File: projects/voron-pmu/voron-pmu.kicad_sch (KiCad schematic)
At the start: 11 parts, among them J1 Critical loads, J2 Non-critical loads, J3 Critical supply, J4 Non-critical supply, K1 FINDER-40.52, K2 FINDER-40.52, K3 FINDER-40.52, K4 FINDER-40.52, SW1 SW_Push, SW2 SW_Push_Open

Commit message: Playing around.
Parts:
- added J5: Pwr-loss-1, Connector_JST:JST_XH_B3B-XH-A_1x03_P2.50mm_Vertical, symbol Connector:Conn_01x03_Pin
- added J6: Pwr-loss-2, Connector_Phoenix_MC:PhoenixContact_MCV_1,5_3-G-3.5_1x03_P3.50mm_Vertical, symbol Connector:Conn_01x03_Pin
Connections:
- net at K4.11: now also J5.2 (Pin_2)
- net at K4.12: now also J5.3 (Pin_3)
- net at K4.14: now also J5.1 (Pin_1)
- net at K4.21: now also J6.2 (Pin_2)
- net at K4.22: now also J6.3 (Pin_3)
- net at K4.24: now also J6.1 (Pin_1)
- net at PS2.5 (AC(L)): now also J3.1 (Pin_1), K1.11
- net at PS2.6 (AC(N)): now also J3.2 (Pin_2), K1.21

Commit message: Prettyfing schematics.
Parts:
- added H1, H2, H3, H4: MountingHole, MountingHole:MountingHole_3.2mm_M3, symbol Mechanical:MountingHole
- J6: footprint Connector_Phoenix_MC:PhoenixContact_MCV_1,5_3-G-3.5_1x03_P3.50mm_Vertical -> Connector_JST:JST_XH_B3B-XH-A_1x03_P2.50mm_Vertical
- SW1: value SW_Push -> sw-on; footprint Connector_Phoenix_MC:PhoenixContact_MCV_1,5_2-G-3.5_1x02_P3.50mm_Vertical -> Connector_JST:JST_XH_B2B-XH-A_1x02_P2.50mm_Vertical
- SW2: value SW_Push_Open -> sw-off; footprint Connector_Phoenix_MC:PhoenixContact_MCV_1,5_2-G-3.5_1x02_P3.50mm_Vertical -> Connector_JST:JST_XH_B2B-XH-A_1x02_P2.50mm_Vertical
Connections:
- net at J3.1 (Pin_1), K1.11: now also PS2.6 (AC(N)); no longer PS2.5 (AC(L))
- net at J3.2 (Pin_2), K1.21: now also PS2.5 (AC(L)); no longer PS2.6 (AC(N))
- net power-good renamed +24V-sw
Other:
- note added: "Critical loads"
- note added: "Low-voltage supply"
- note added: "Main power on/off switching"
- note added: "Non-critical loads and detection"
- moved on the sheet: J1, J2, J3, J4, J5, J6, K1, K2, K3, K4, PS2, SW1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

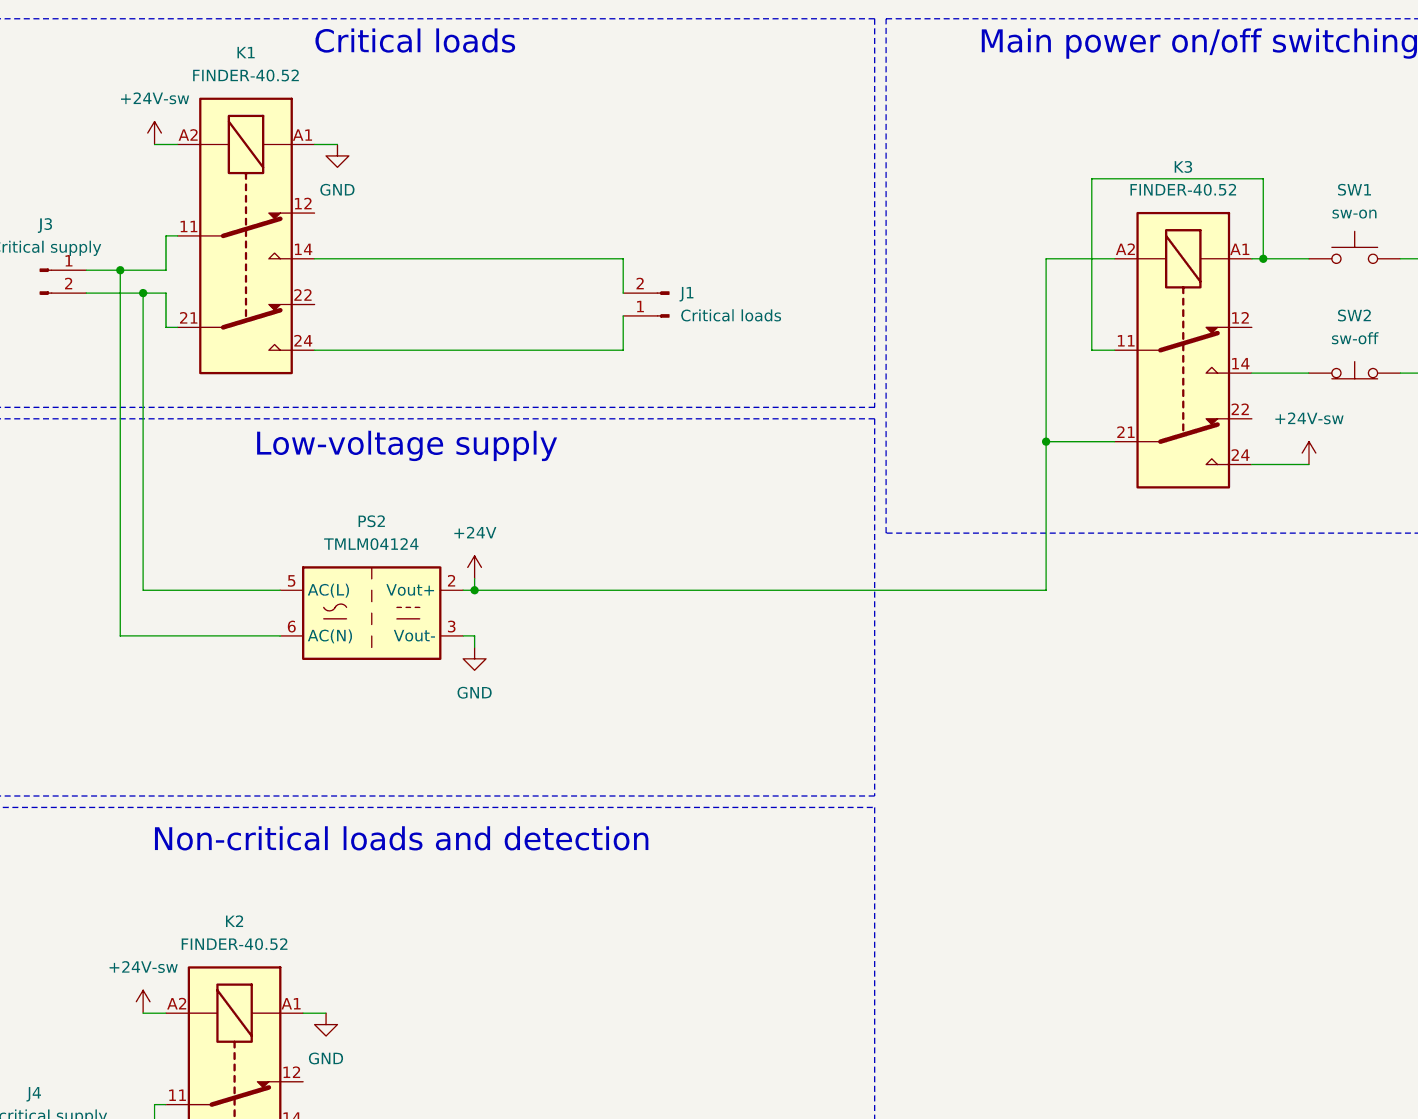
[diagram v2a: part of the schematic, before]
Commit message: Replacing relays with Omron. Will route now.
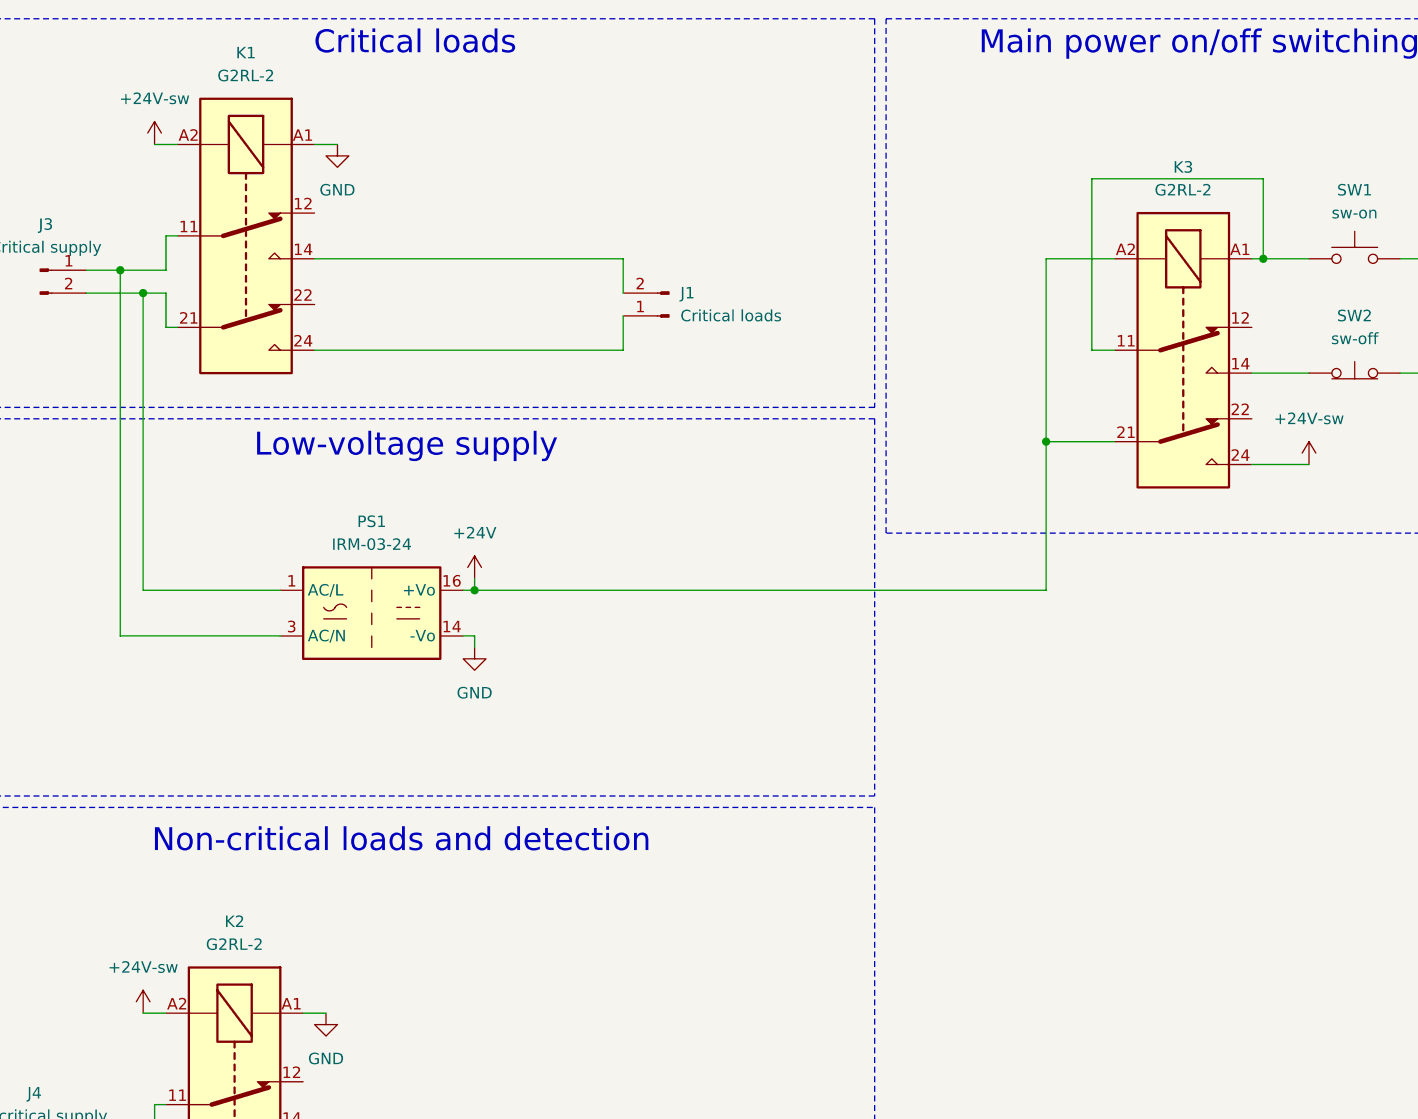
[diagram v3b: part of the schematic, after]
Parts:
- K1, K2, K3: value FINDER-40.52 -> G2RL-2; footprint Relay_THT:Relay_DPDT_Finder_40.52 -> Relay_THT:Relay_DPDT_Omron_G2RL-2; symbol Relay:FINDER-40.52 -> Relay:G2RL-2
- PS1: renamed from PS2; value TMLM04124 -> IRM-03-24; footprint Converter_ACDC:Converter_ACDC_TRACO_TMLM-04_THT -> Converter_ACDC:Converter_ACDC_MeanWell_IRM-03-xx_THT; symbol Converter_ACDC:TMLM04124 -> Converter_ACDC:IRM-03-24
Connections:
- net +24V: now also PS1.16 (+Vo); no longer PS1.2 (Vout+)
- net GND: now also PS1.14 (-Vo); no longer PS1.3 (Vout-)
- net at J3.2 (Pin_2), K1.21: now also PS1.1 (AC/L); no longer PS1.5 (AC(L))
- net at J3.1 (Pin_1), K1.11: now also PS1.3 (AC/N); no longer PS1.6 (AC(N))
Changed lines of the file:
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@@
 	)
 	(symbol
-		(lib_id "Converter_ACDC:TMLM04124")
+		(lib_id "Converter_ACDC:IRM-03-24")
 		(at 63.5 82.55 0)
 		(unit 1)
@@
 		(dnp no)
 		(fields_autoplaced yes)
-		(property "Reference" "PS2"
+		(property "Reference" "PS1"
 			(at 63.5 72.39 0)
 			(effects
@@
 			)
 		)
-		(property "Value" "TMLM04124"
+		(property "Value" "IRM-03-24"
 			(at 63.5 74.93 0)
 			(effects
@@
 			)
 		)
-		(property "Footprint" "Converter_ACDC:Converter_ACDC_TRACO_TMLM-04_THT"
+		(property "Footprint" "Converter_ACDC:Converter_ACDC_MeanWell_IRM-03-xx_THT"
 			(at 63.5 91.44 0)
 			(effects
@@
 			)
 		)
-		(property "Datasheet" "https://www.tracopower.com/products/tmlm.pdf"
+		(property "Datasheet" "https://www.meanwell.com/Upload/PDF/IRM-03/IRM-03-SPEC.PDF"
+			(at 63.5 92.71 0)
+			(effects
+				(font
+					(size 1.27 1.27)
+				)
+				(hide yes)
+			)
+		)
+		(property "Description" "24V, 125mA, 3W, Isolated, AC-DC, IRM03"
 			(at 63.5 82.55 0)
 			(effects
@@
 			)
 		)
-		(property "Description" "24V 167mA AC/DC low noise power module"
-			(at 63.5 82.55 0)
-			(effects
-				(font
-					(size 1.27 1.27)
-				)
-				(hide yes)
-			)
-		)
 		(pin "3"
 		)
-		(pin "2"
-		)
-		(pin "6"
+		(pin "1"
+		)
+		(pin "16"
 		)
 		(pin "5"
 		)
-		(instances
-			(project "voron-pmu"
-				(path "/2cf7b3ca-ad8f-4a14-9215-f0584bf5d4a1"
-					(reference "PS2")
+		(pin "14"
+		)
+		(instances
+			(project "voron-pmu"
+				(path "/2cf7b3ca-ad8f-4a14-9215-f0584bf5d4a1"
+					(reference "PS1")
 					(unit 1)
 				)
@@
 	)
 	(symbol
-		(lib_id "Relay:FINDER-40.52")
+		(lib_id "Relay:G2RL-2")
 		(at 48.26 137.16 270)
 		(unit 1)
@@
 			)
 		)
-		(property "Value" "FINDER-40.52"
+		(property "Value" "G2RL-2"
 			(at 48.26 119.38 90)
 			(effects
@@
 			)
 		)
-		(property "Footprint" "Relay_THT:Relay_DPDT_Finder_40.52"
-			(at 47.498 171.45 0)
-			(effects
-				(font
-					(size 1.27 1.27)
-				)
-				(hide yes)
-			)
-		)
-		(property "Datasheet" "http://gfinder.findernet.com/assets/Series/353/S40EN.pdf"
+		(property "Footprint" "Relay_THT:Relay_DPDT_Omron_G2RL-2"
+			(at 46.99 153.67 0)
+			(effects
+				(font
+					(size 1.27 1.27)
+				)
+				(justify left)
+				(hide yes)
+			)
+		)
+		(property "Datasheet" "https://omronfs.omron.com/en_US/ecb/products/pdf/en-g2rl.pdf"
 			(at 48.26 137.16 0)
 			(effects
@@
 			)
 		)
-		(property "Description" "FINDER 40.52, Dual Pole Relay, 5mm Pitch, 10A"
+		(property "Description" "General Purpose Low Profile Relay DPDT Through Hole, Omron G2RL series, 8A 250VAC"
 			(at 48.26 137.16 0)
 			(effects
@@
 	)
 	(symbol
-		(lib_id "Relay:FINDER-40.52")
+		(lib_id "Relay:G2RL-2")
 		(at 49.53 40.64 270)
 		(unit 1)
@@
 			)
 		)
-		(property "Value" "FINDER-40.52"
+		(property "Value" "G2RL-2"
 			(at 49.53 22.86 90)
 			(effects
@@
 			)
 		)
-		(property "Footprint" "Relay_THT:Relay_DPDT_Finder_40.52"
-			(at 48.768 74.93 0)
-			(effects
-				(font
-					(size 1.27 1.27)
-				)
-				(hide yes)
-			)
-		)
-		(property "Datasheet" "http://gfinder.findernet.com/assets/Series/353/S40EN.pdf"
+		(property "Footprint" "Relay_THT:Relay_DPDT_Omron_G2RL-2"
+			(at 48.26 57.15 0)
+			(effects
+				(font
+					(size 1.27 1.27)
+				)
+				(justify left)
+				(hide yes)
+			)
+		)
+		(property "Datasheet" "https://omronfs.omron.com/en_US/ecb/products/pdf/en-g2rl.pdf"
 			(at 49.53 40.64 0)
 			(effects
@@
 			)
 		)
-		(property "Description" "FINDER 40.52, Dual Pole Relay, 5mm Pitch, 10A"
+		(property "Description" "General Purpose Low Profile Relay DPDT Through Hole, Omron G2RL series, 8A 250VAC"
 			(at 49.53 40.64 0)
 			(effects
@@
 	)
 	(symbol
-		(lib_id "Relay:FINDER-40.52")
+		(lib_id "Relay:G2RL-2")
 		(at 153.67 53.34 270)
 		(unit 1)
@@
 			)
 		)
-		(property "Value" "FINDER-40.52"
+		(property "Value" "G2RL-2"
 			(at 153.67 35.56 90)
 			(effects
@@
 			)
 		)
-		(property "Footprint" "Relay_THT:Relay_DPDT_Finder_40.52"
-			(at 152.908 87.63 0)
-			(effects
-				(font
-					(size 1.27 1.27)
-				)
-				(hide yes)
-			)
-		)
-		(property "Datasheet" "http://gfinder.findernet.com/assets/Series/353/S40EN.pdf"
+		(property "Footprint" "Relay_THT:Relay_DPDT_Omron_G2RL-2"
+			(at 152.4 69.85 0)
+			(effects
+				(font
+					(size 1.27 1.27)
+				)
+				(justify left)
+				(hide yes)
+			)
+		)
+		(property "Datasheet" "https://omronfs.omron.com/en_US/ecb/products/pdf/en-g2rl.pdf"
 			(at 153.67 53.34 0)
 			(effects
@@
 			)
 		)
-		(property "Description" "FINDER 40.52, Dual Pole Relay, 5mm Pitch, 10A"
+		(property "Description" "General Purpose Low Profile Relay DPDT Through Hole, Omron G2RL series, 8A 250VAC"
 			(at 153.67 53.34 0)
 			(effects

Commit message: Battling Mouser and Kicad.
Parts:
- PS1: value IRM-03-24 -> RAC05-24SK; footprint Converter_ACDC:Converter_ACDC_MeanWell_IRM-03-xx_THT -> Converter_ACDC:Converter_ACDC_RECOM_RAC05-xxSK_THT; symbol Converter_ACDC:IRM-03-24 -> Converter_ACDC:RAC05-24SK
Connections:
- net +24V: now also PS1.5 (+Vout); no longer PS1.16 (+Vo)
- net GND: now also PS1.4 (-Vout); no longer PS1.14 (-Vo)
- net at J3.1 (Pin_1), K1.11: now also PS1.2 (AC(N)); no longer PS1.3 (AC/N)
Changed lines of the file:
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@@
 	)
 	(symbol
-		(lib_id "Converter_ACDC:IRM-03-24")
+		(lib_id "Converter_ACDC:RAC05-24SK")
 		(at 63.5 82.55 0)
 		(unit 1)
@@
 			)
 		)
-		(property "Value" "IRM-03-24"
+		(property "Value" "RAC05-24SK"
 			(at 63.5 74.93 0)
 			(effects
@@
 			)
 		)
-		(property "Footprint" "Converter_ACDC:Converter_ACDC_MeanWell_IRM-03-xx_THT"
+		(property "Footprint" "Converter_ACDC:Converter_ACDC_RECOM_RAC05-xxSK_THT"
 			(at 63.5 91.44 0)
 			(effects
@@
 			)
 		)
-		(property "Datasheet" "https://www.meanwell.com/Upload/PDF/IRM-03/IRM-03-SPEC.PDF"
-			(at 63.5 92.71 0)
+		(property "Datasheet" "https://www.recom-power.com/pdf/Powerline-AC-DC/RAC05-K.pdf"
+			(at 60.96 74.93 0)
 			(effects
 				(font
@@
 			)
 		)
-		(property "Description" "24V, 125mA, 3W, Isolated, AC-DC, IRM03"
+		(property "Description" "5W Single Output EMC Class B 24V 210mA"
 			(at 63.5 82.55 0)
 			(effects
@@
 		(pin "1"
 		)
-		(pin "16"
+		(pin "2"
 		)
 		(pin "5"
 		)
-		(pin "14"
+		(pin "4"
 		)
 		(instances
